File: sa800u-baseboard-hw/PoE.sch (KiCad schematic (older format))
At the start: 24 parts, among them IC2 TPS2378DDA

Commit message: Review - Add geeral remarks
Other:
- note added: "REMARK: What is the purpose of these PWR_FLAGS? \neeeeIf it is intended as a test point use TP_SMD1MM instead."
- note added: "REMARK:Typical aplication circuit can be found in \nTPS2378DDA datasheet:\n https://www.ti.com/lit/ds/symlink/tps2378.pdf?ts=1637556069032&ref_url=https%253A%252F%252Fwww.google.com%252F\nThere is the reference connection for APD circuit."
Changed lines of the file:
@@
 Text GLabel 7250 2100 2    50   Input ~ 0
 APD
-Text Notes 5100 1700 0    50   ~ 0
+Text Notes 4975 1675 0    50   ~ 0
 What about APD? This circuit may be powered from other than PoE source.
 Wire Wire Line
@@
 Wire Wire Line
 	6100 4900 6100 5100
+Text Notes 5275 1325 0    50   ~ 0
+REMARK:Typical aplication circuit can be found in \nTPS2378DDA datasheet:\n https://www.ti.com/lit/ds/symlink/tps2378.pdf?ts=1637556069032&ref_url=https%253A%252F%252Fwww.google.com%252F\nThere is the reference connection for APD circuit.
+Text Notes 3775 3275 0    50   ~ 0
+REMARK: What is the purpose of these PWR_FLAGS? \neeeeIf it is intended as a test point use TP_SMD1MM instead.
 $EndSCHEMATC

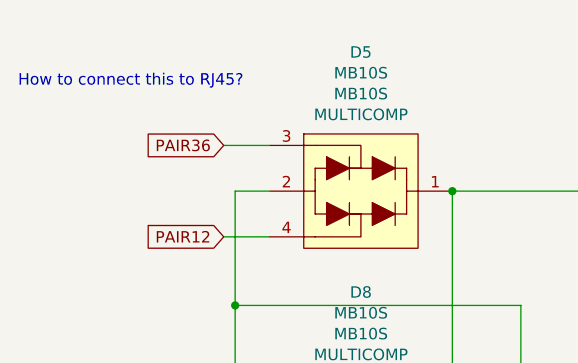
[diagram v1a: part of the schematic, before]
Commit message: fixed ethernet controller symbol
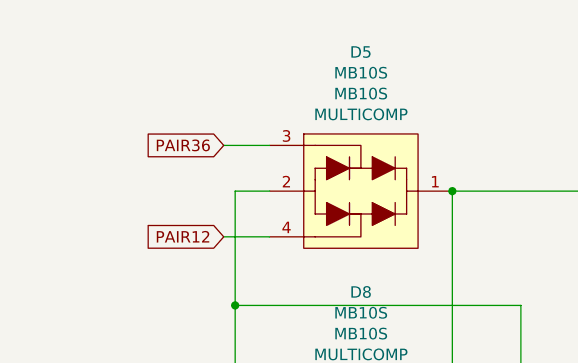
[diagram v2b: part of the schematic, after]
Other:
- note removed: "How to connect this to RJ45?"
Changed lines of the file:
@@
 	1    0    0    -1
 $EndComp
-Text Notes 550  1300 0    50   ~ 0
-How to connect this to RJ45?
 Wire Wire Line
 	1850 4750 1850 5100

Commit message: introducing minor genreal improvements
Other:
- note removed: "REMARK: What is the purpose of these PWR_FLAGS? \neeeeIf it is intended as a test point use TP_SMD1MM instead."
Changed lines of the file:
@@
 	5750 1750 7950 1750
-Wire Wire Line
-	1850 5500 2200 5500
-$Comp
-L power:PWR_FLAG #FLG0101
-U 1 1 61A82610
-P 4700 1750
-F 0 "#FLG0101" H 4700 1825 50  0001 C CNN
-F 1 "PWR_FLAG" H 4700 1923 50  0000 C CNN
-F 2 "" H 4700 1750 50  0001 C CNN
-F 3 "~" H 4700 1750 50  0001 C CNN
-	1    4700 1750
-	1    0    0    -1
-$EndComp
-$Comp
-L power:PWR_FLAG #FLG0102
-U 1 1 61A95F09
-P 2200 5500
-F 0 "#FLG0102" H 2200 5575 50  0001 C CNN
-F 1 "PWR_FLAG" H 2200 5673 50  0000 C CNN
-F 2 "" H 2200 5500 50  0001 C CNN
-F 3 "~" H 2200 5500 50  0001 C CNN
-	1    2200 5500
-	-1   0    0    1
-$EndComp
-Connection ~ 2200 5500
-Wire Wire Line
-	2200 5500 2950 5500
 Wire Wire Line
 	6750 2200 7450 2200
@@
 Wire Wire Line
 	6750 2100 7250 2100
-$Comp
-L power:PWR_FLAG #FLG0103
-U 1 1 61AB6F5B
-P 4700 2900
-F 0 "#FLG0103" H 4700 2975 50  0001 C CNN
-F 1 "PWR_FLAG" H 4700 3073 50  0000 C CNN
-F 2 "" H 4700 2900 50  0001 C CNN
-F 3 "~" H 4700 2900 50  0001 C CNN
-	1    4700 2900
-	-1   0    0    1
-$EndComp
 $Comp
 L antmicroResistors0402:R_0R_0402 R16
@@
 Text Notes 5275 1325 0    50   ~ 0
 REMARK:Typical aplication circuit can be found in \nTPS2378DDA datasheet:\n https://www.ti.com/lit/ds/symlink/tps2378.pdf?ts=1637556069032&ref_url=https%253A%252F%252Fwww.google.com%252F\nThere is the reference connection for APD circuit.
-Text Notes 3775 3275 0    50   ~ 0
-REMARK: What is the purpose of these PWR_FLAGS? \neeeeIf it is intended as a test point use TP_SMD1MM instead.
+Wire Wire Line
+	1850 5500 2950 5500
 $EndSCHEMATC

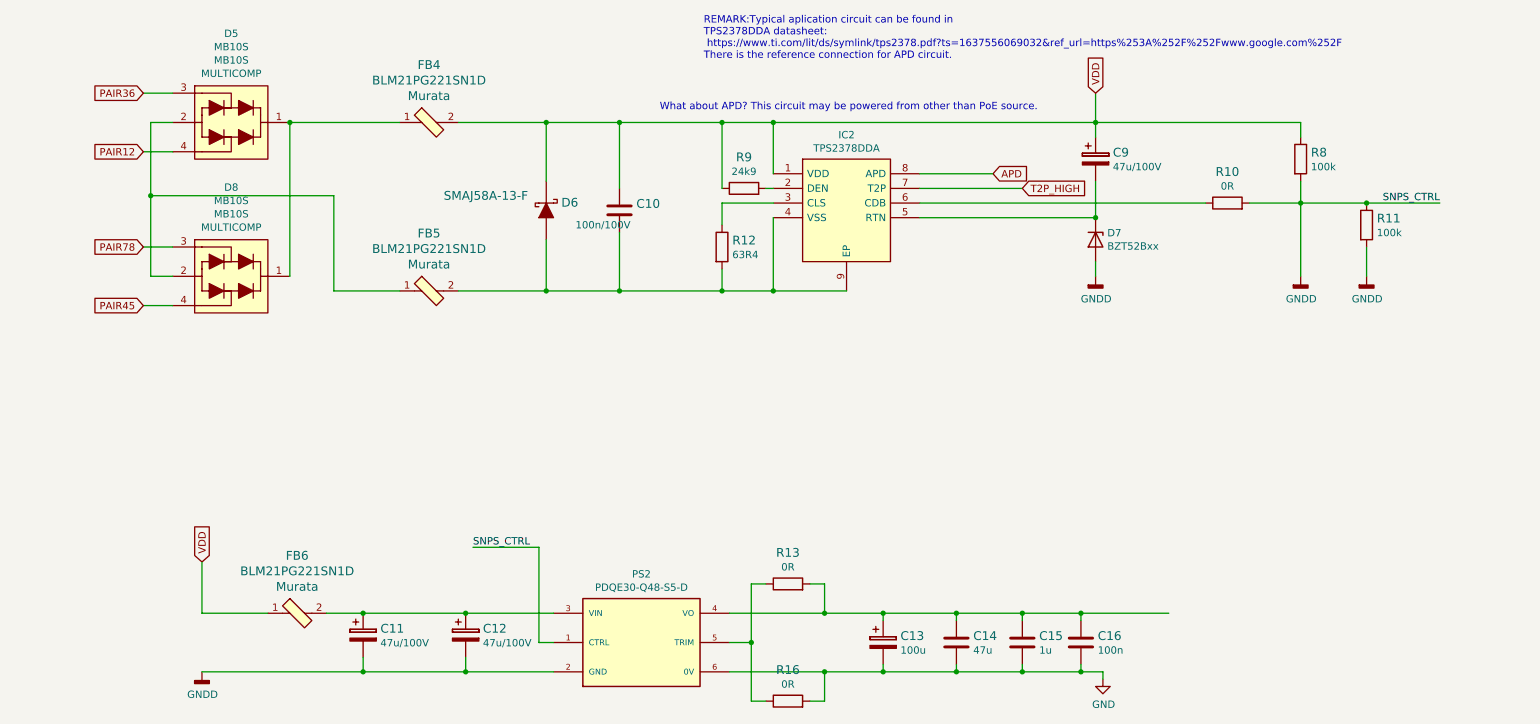
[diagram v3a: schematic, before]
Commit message: fixed / unified power labels
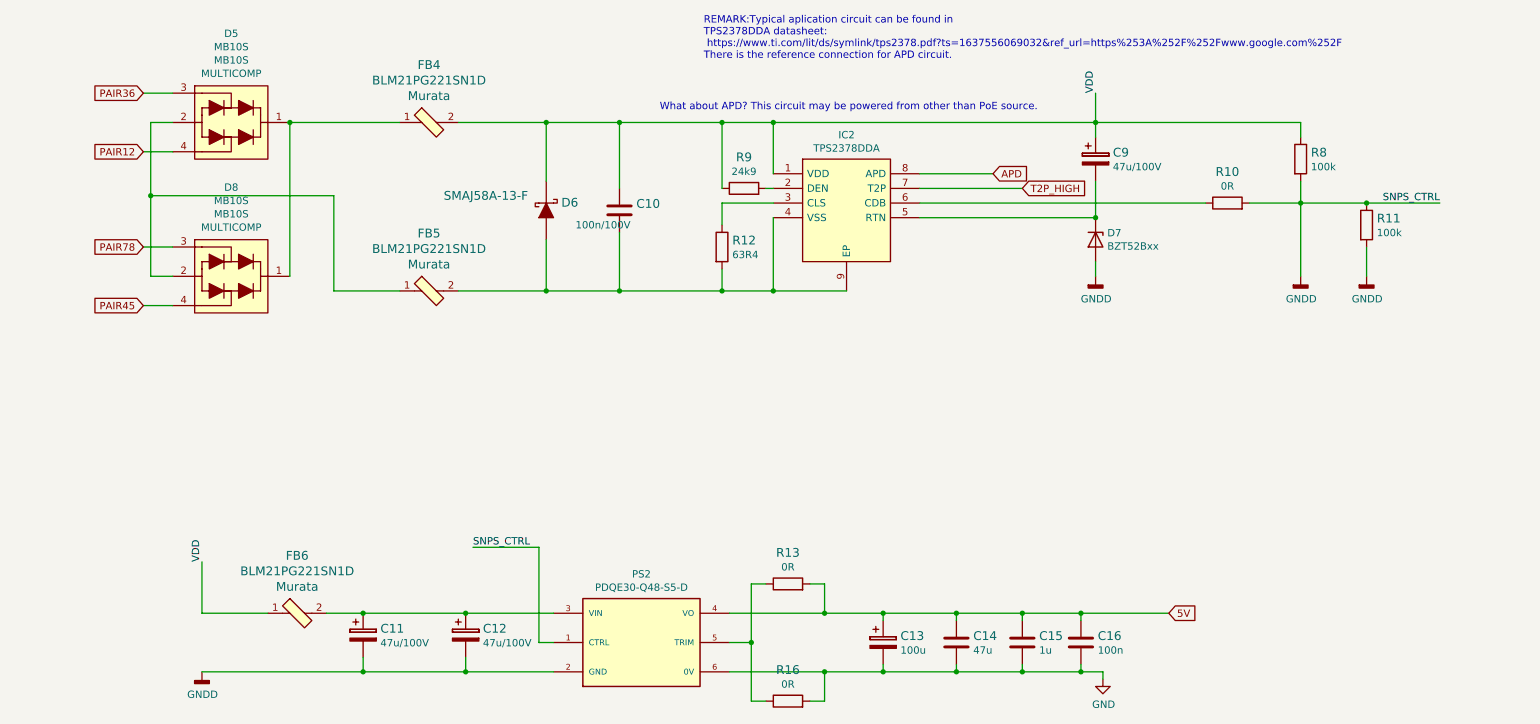
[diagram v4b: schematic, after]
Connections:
- net 5V: now reaches C13.1, C14.1, C15.1, C16.1, PS2.4 (VO), R13.2
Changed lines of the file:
@@
 Wire Wire Line
 	1850 5100 2300 5100
-Text GLabel 1850 4750 1    50   Input ~ 0
-VDD
 Wire Wire Line
 	9800 2600 9800 2800
@@
 Wire Wire Line
 	7950 1750 7950 1550
-Text GLabel 7950 1550 1    50   Input ~ 0
-VDD
 Wire Wire Line
 	7950 2150 7950 2400
@@
 Wire Wire Line
 	1850 5500 2950 5500
+Text GLabel 8450 5100 2    50   Input ~ 0
+5V
+Text Label 7950 1550 1    50   ~ 0
+VDD
+Text Label 1850 4750 1    50   ~ 0
+VDD
 $EndSCHEMATC
